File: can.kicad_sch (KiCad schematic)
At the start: 14 parts, among them J14 CAN, J15 CAN, U22 MCP2562, U23 MCP2515, Y1 8MHz

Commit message: more cleanup and added notes for review
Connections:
- net INT renamed ~{CAN_INTERRUPT}

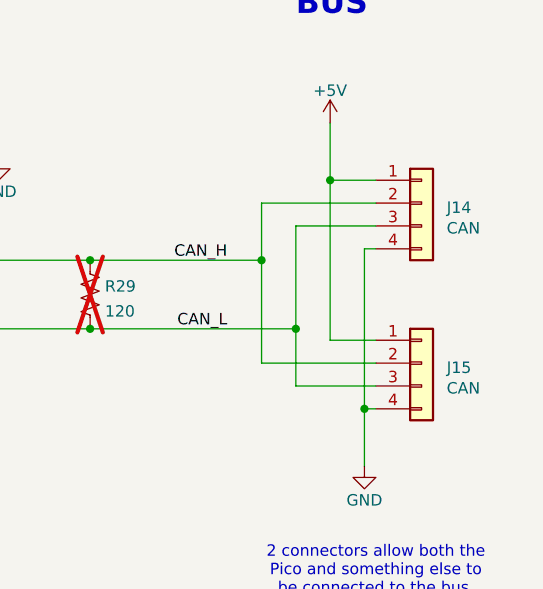
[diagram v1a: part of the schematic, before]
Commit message: DNP unused connectors for now
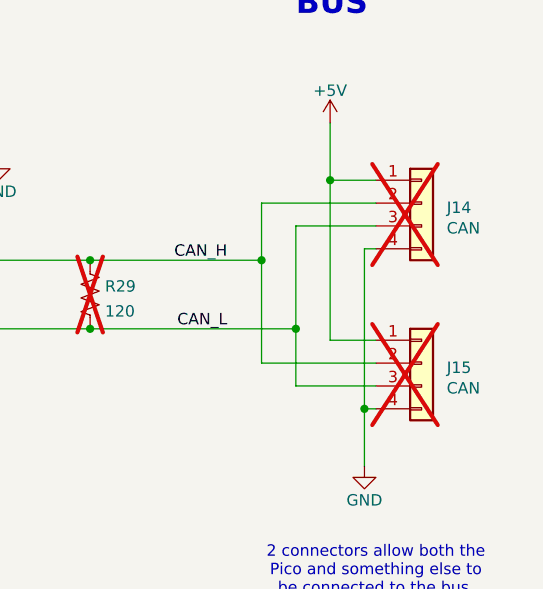
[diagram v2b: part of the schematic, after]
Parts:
- J14, J15: now not fitted
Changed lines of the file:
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@@
 		(in_bom yes)
 		(on_board yes)
-		(dnp no)
+		(dnp yes)
 		(property "Reference" "J15"
 			(at 242.824 104.648 0)
@@
 		(in_bom yes)
 		(on_board yes)
-		(dnp no)
+		(dnp yes)
 		(property "Reference" "J14"
 			(at 242.824 86.868 0)

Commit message: major rework again after the meeting
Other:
- note removed: "Also shifts from 3V3 to 5V."
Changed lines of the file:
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@@
-		)
-	)
-	(text "Also shifts from 3V3 to 5V."
-		(exclude_from_sim no)
-		(at 166.878 117.602 0)
-		(effects
-			(font
-				(size 1.27 1.27)
-			)
-			(justify left bottom)
 		)
 	)
 	(text "2 connectors allow both the\nPico and something else to\nbe connected to the bus."
 		(exclude_from_sim no)
-		(at 234.95 127.254 0)
+		(at 210.312 117.348 0)
 		(effects
 			(font

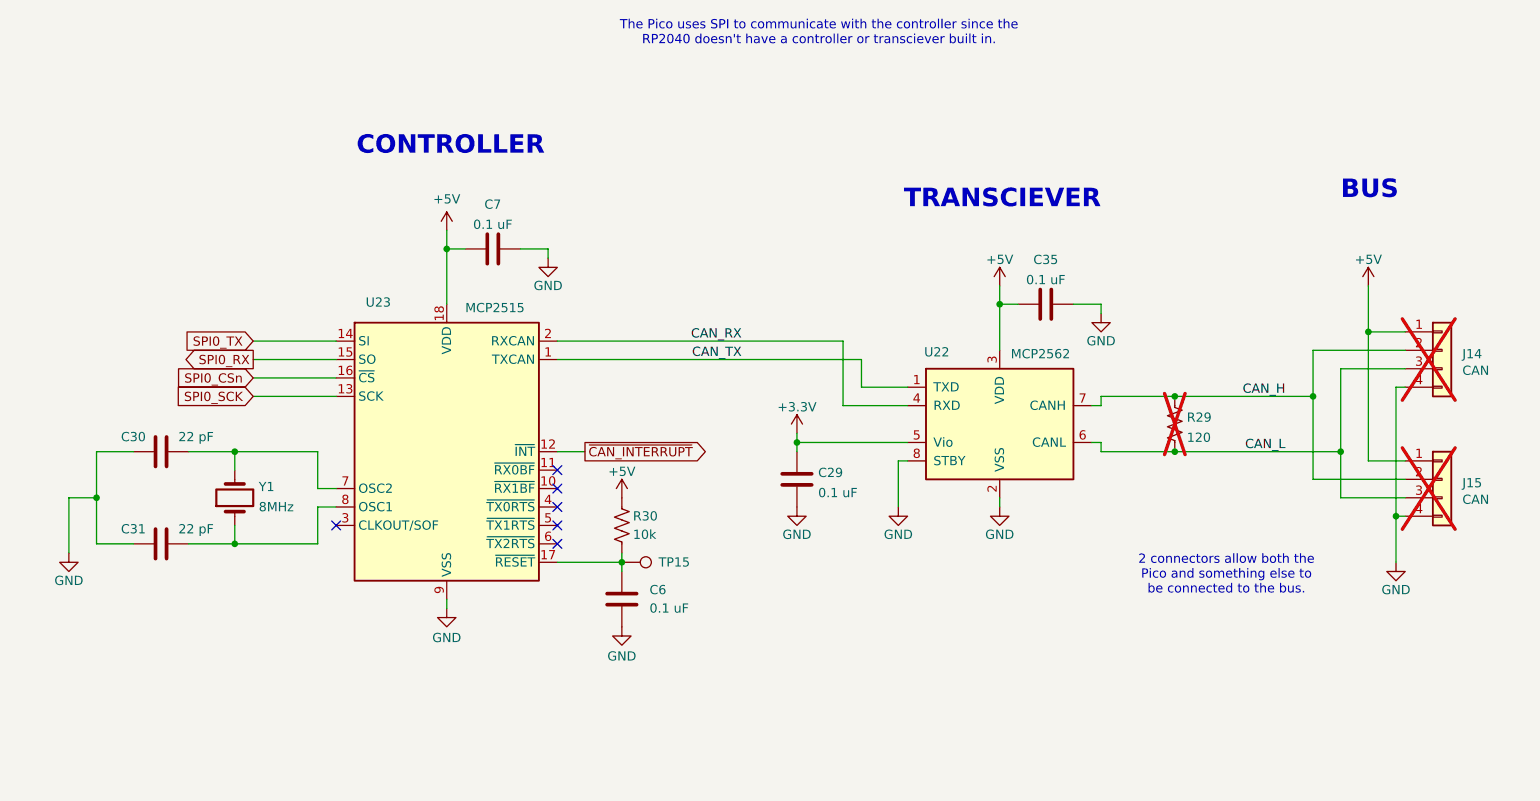
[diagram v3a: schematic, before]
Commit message: major finishing touches:     - major rework for v5.1     - silkscreen and stuff     - impednace for USB and CAN lines     - schematic comments     - symbol, footprint, and model library updates
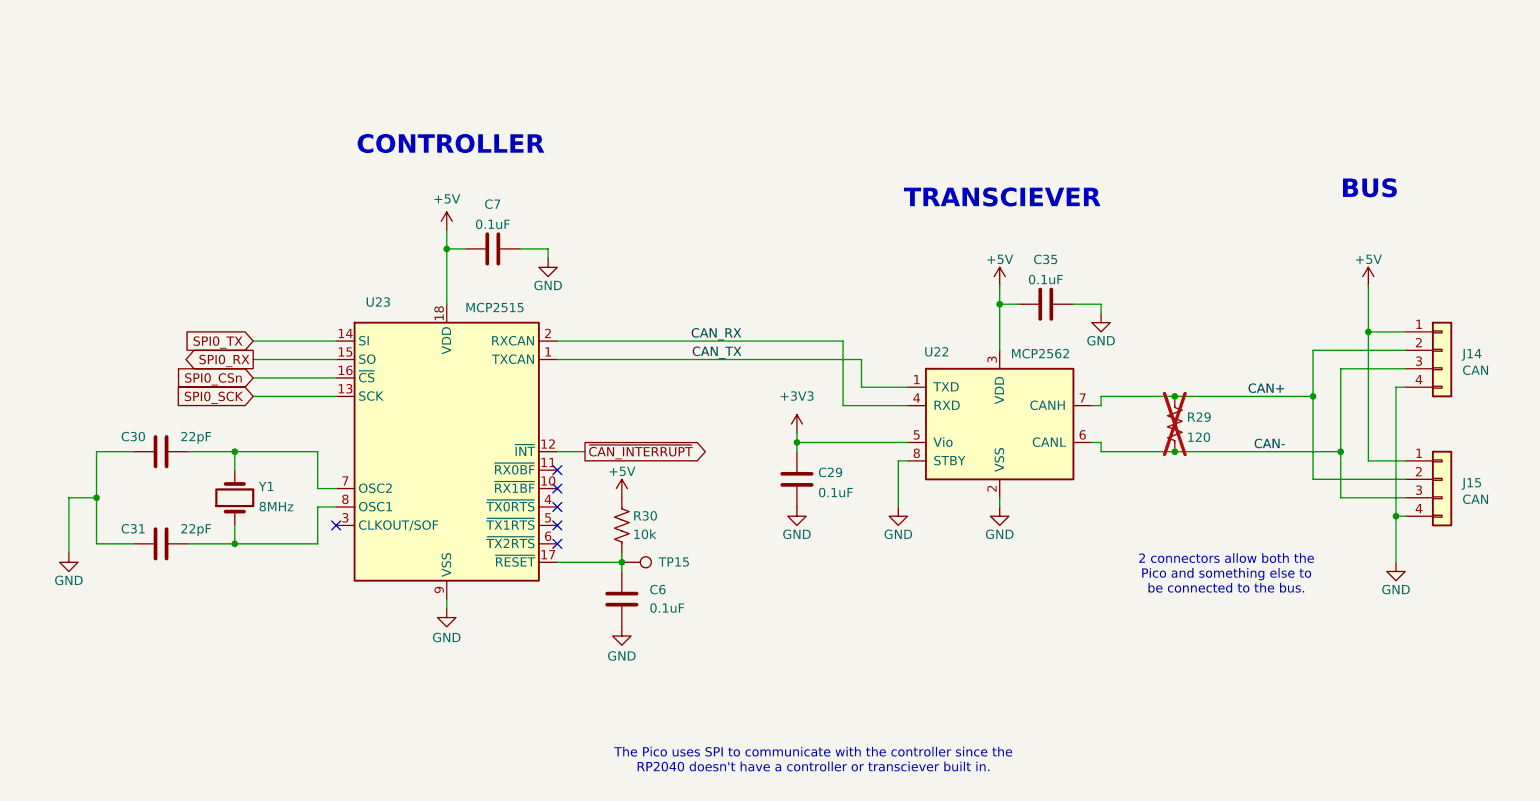
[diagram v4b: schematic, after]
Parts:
- C29, C35, C6, C7: value 0.1 uF -> 0.1uF; Manufacturer (none) -> KEMET; Manufacturer Part Number (none) -> C1206C104J5RACTU; Vendor (none) -> Digikey; Vendor Part Number (none) -> 399-C1206C104J5RACTUCT-ND
- C30, C31: value 22 pF -> 22pF; Manufacturer (none) -> KEMET; Manufacturer Part Number (none) -> C0603C220K5RACTU; Vendor (none) -> Digikey; Vendor Part Number (none) -> 399-C0603C220K5RACTUCT-ND
- J14, J15: Manufacturer (none) -> Molex; Manufacturer Part Number (none) -> 0530470410; Vendor (none) -> Digikey; Vendor Part Number (none) -> WM1733-ND; now fitted
- R29: footprint Resistor_SMD:R_0805_2012Metric_Pad1.20x1.40mm_HandSolder -> Resistor_SMD:R_0603_1608Metric_Pad0.98x0.95mm_HandSolder; Manufacturer (none) -> Stackpole Electronics Inc; Manufacturer Part Number (none) -> RNCP0603FTD121R; Vendor (none) -> Digikey; Vendor Part Number (none) -> RNCP0603FTD121RCT-ND
- R30: footprint Resistor_SMD:R_0805_2012Metric_Pad1.20x1.40mm_HandSolder -> Resistor_SMD:R_0603_1608Metric_Pad0.98x0.95mm_HandSolder; Manufacturer (none) -> Stackpole Electronics Inc; Manufacturer Part Number (none) -> RNCP0603FTD10K0; Vendor (none) -> Digikey; Vendor Part Number (none) -> RNCP0603FTD10K0CT-ND
- TP15: now left out of the parts list
- U22: Manufacturer (none) -> Microchip Technology; Manufacturer Part Number (none) -> MCP2562FDT-E/SN; Vendor (none) -> Digikey; Vendor Part Number (none) -> MCP2562FDT-E/SNCT-ND
- U23: Manufacturer (none) -> Microchip Technology; Manufacturer Part Number (none) -> MCP2515T-E/SO; Vendor (none) -> Digikey; Vendor Part Number (none) -> MCP2515T-E/SOCT-ND
- Y1: Manufacturer (none) -> Würth Elektronik; Manufacturer Part Number (none) -> 830003151; Vendor (none) -> Digikey; Vendor Part Number (none) -> 732-830003151CT-ND
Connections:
- net +3.3V renamed +3V3
- net CAN_H renamed CAN+
- net CAN_L renamed CAN-
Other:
- company: WVU Unviersity Rover Challenge -> WVU Unviersity Rover Challenge (URC)

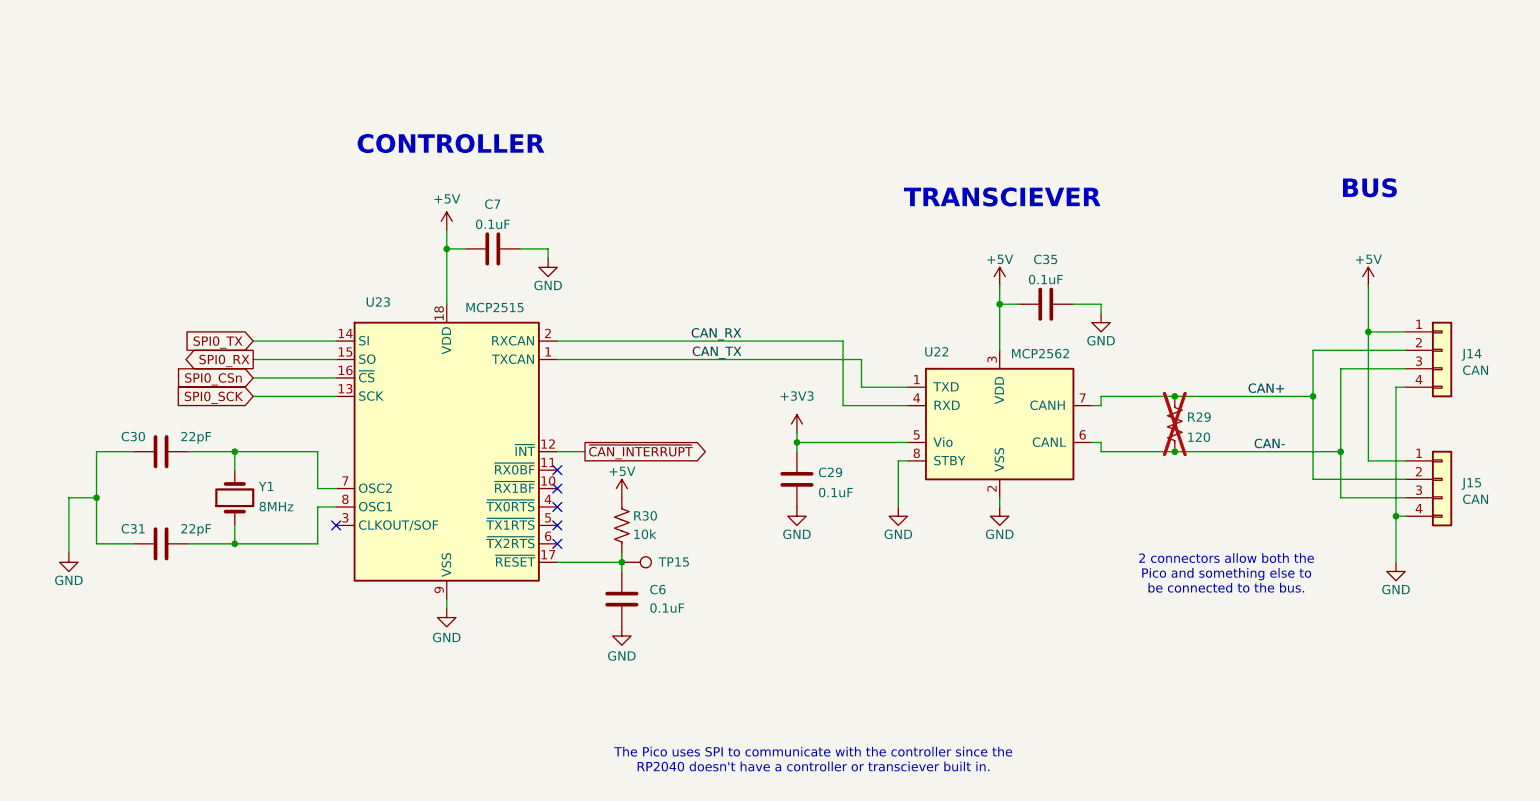
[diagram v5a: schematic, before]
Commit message: swapped UART to USB from FTDI (out of stock) to MCP2200
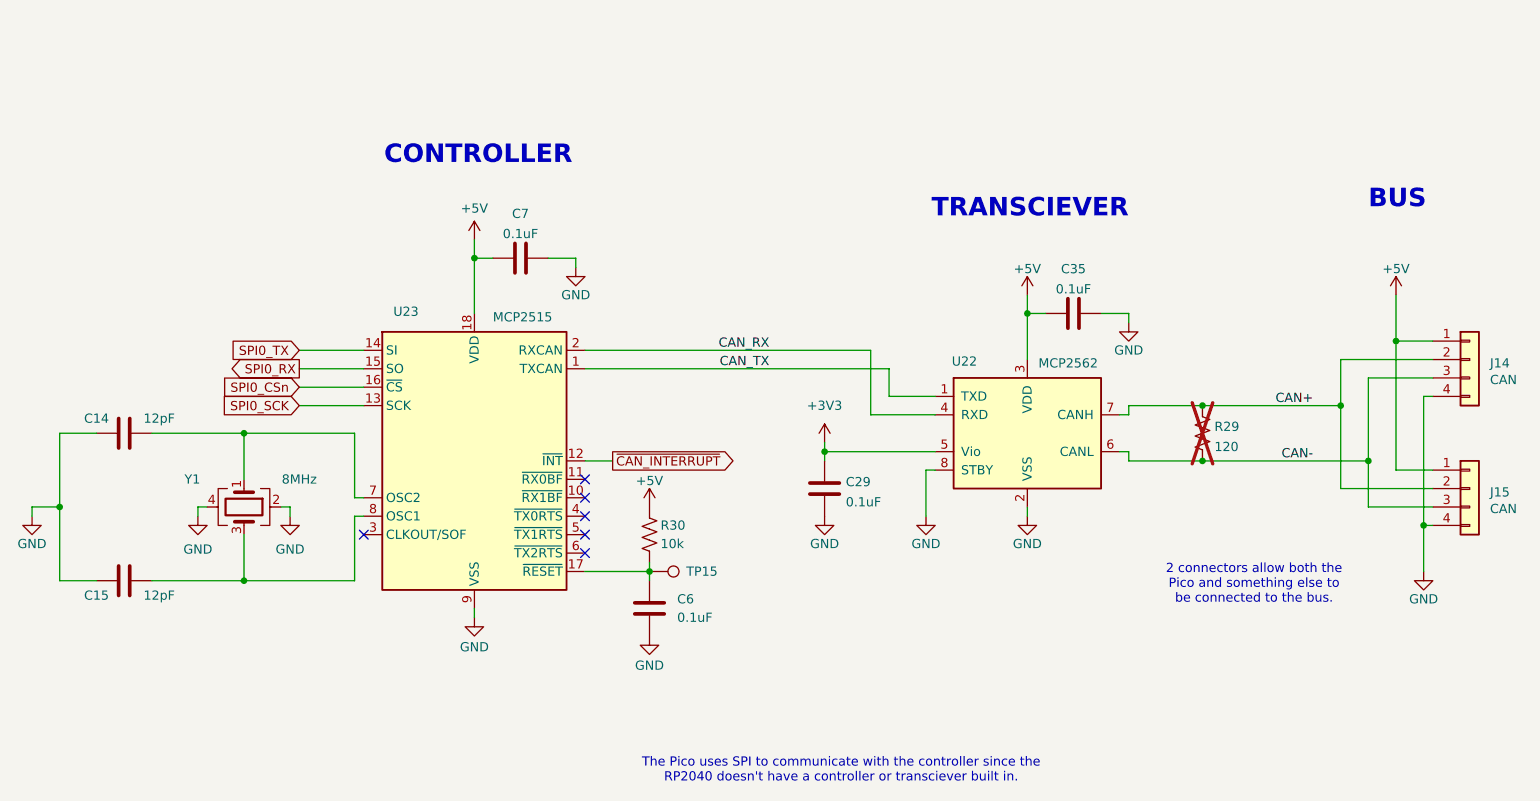
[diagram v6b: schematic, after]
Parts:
- removed C30, C31: 22pF, Capacitor_SMD:C_0603_1608Metric_Pad1.08x0.95mm_HandSolder, symbol Device:C
- removed Y1: 8MHz, Crystal:Crystal_SMD_HC49-SD, symbol Device:Crystal
- added C14, C15: 12pF, Capacitor_SMD:C_0603_1608Metric_Pad1.08x0.95mm_HandSolder, symbol Device:C
- added Y1: 8MHz, Crystal:Crystal_SMD_3225-4Pin_3.2x2.5mm, symbol Device:Crystal_GND24
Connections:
- net GND: now also C14.1, C15.1, Y1.2, Y1.4
- net at U23.8 (OSC1): now also C15.2, Y1.3
- net at U23.7 (OSC2): now also C14.2, Y1.1
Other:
- moved on the sheet: C29, C35, C6, C7, J14, J15, R29, R30, TP15, U22, U23

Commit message: Added housing/cable/header info to each connector's symbol properties.
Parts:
- J14, J15: Cable (none) -> 0500798000-06-B6; Housing (none) -> 0510210400
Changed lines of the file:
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@@
+			)
+		)
+		(property "Housing" ""
+			(at 207.01 97.79 0)
+			(effects
+				(font
+					(size 1.27 1.27)
+				)
+				(hide yes)
 			)
 		)
@@
 			)
 		)
+		(property "Housing" ""
+			(at 130.81 111.76 0)
+			(effects
+				(font
+					(size 1.27 1.27)
+				)
+				(hide yes)
+			)
+		)
 		(pin "1"
 		)
@@
 			)
 		)
+		(property "Housing" ""
+			(at 58.42 97.79 90)
+			(effects
+				(font
+					(size 1.27 1.27)
+				)
+				(hide yes)
+			)
+		)
 		(pin "1"
 		)
@@
 		)
 		(property "Notes" ""
+			(at 243.84 105.41 0)
+			(effects
+				(font
+					(size 1.27 1.27)
+				)
+				(hide yes)
+			)
+		)
+		(property "Housing" "0510210400"
+			(at 243.84 105.41 0)
+			(effects
+				(font
+					(size 1.27 1.27)
+				)
+				(hide yes)
+			)
+		)
+		(property "Cable" "0500798000-06-B6"
 			(at 243.84 105.41 0)
 			(effects
@@
 			)
 		)
+		(property "Housing" ""
+			(at 154.94 105.41 0)
+			(effects
+				(font
+					(size 1.27 1.27)
+				)
+				(hide yes)
+			)
+		)
 		(pin "1"
 		)
@@
 			)
 		)
+		(property "Housing" ""
+			(at 189.23 81.28 90)
+			(effects
+				(font
+					(size 1.27 1.27)
+				)
+				(hide yes)
+			)
+		)
 		(pin "1"
 		)
@@
 			)
 		)
+		(property "Housing" ""
+			(at 58.42 118.11 90)
+			(effects
+				(font
+					(size 1.27 1.27)
+				)
+				(hide yes)
+			)
+		)
 		(pin "1"
 		)
@@
 			)
 		)
+		(property "Housing" ""
+			(at 113.03 73.66 90)
+			(effects
+				(font
+					(size 1.27 1.27)
+				)
+				(hide yes)
+			)
+		)
 		(pin "1"
 		)
@@
 			)
 		)
+		(property "Housing" ""
+			(at 182.88 97.79 0)
+			(effects
+				(font
+					(size 1.27 1.27)
+				)
+				(hide yes)
+			)
+		)
 		(pin "1"
 		)
@@
 		)
 		(property "Notes" ""
+			(at 106.68 101.6 0)
+			(effects
+				(font
+					(size 1.27 1.27)
+				)
+				(hide yes)
+			)
+		)
+		(property "Housing" ""
 			(at 106.68 101.6 0)
 			(effects
@@
 			)
 		)
+		(property "Housing" ""
+			(at 130.81 116.84 90)
+			(effects
+				(font
+					(size 1.27 1.27)
+				)
+				(hide yes)
+			)
+		)
 		(pin "1"
 		)
@@
 		)
 		(property "Notes" ""
+			(at 243.84 87.63 0)
+			(effects
+				(font
+					(size 1.27 1.27)
+				)
+				(hide yes)
+			)
+		)
+		(property "Housing" "0510210400"
+			(at 243.84 87.63 0)
+			(effects
+				(font
+					(size 1.27 1.27)
+				)
+				(hide yes)
+			)
+		)
+		(property "Cable" "0500798000-06-B6"
 			(at 243.84 87.63 0)
 			(effects
@@
 			)
 		)
+		(property "Housing" ""
+			(at 130.81 121.92 0)
+			(effects
+				(font
+					(size 1.27 1.27)
+				)
+				(hide yes)
+			)
+		)
 		(pin "1"
 		)
@@
 			(at 74.93 107.95 90)
 			(effects
+				(font
+					(size 1.27 1.27)
+				)
+				(hide yes)
+			)
+		)
+		(property "Housing" ""
+			(at 74.93 107.95 90)
+			(effects
